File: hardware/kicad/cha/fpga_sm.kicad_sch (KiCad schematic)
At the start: 26 parts, among them J3 CONF SM, U14 iCE40HX4K-TQ144, X2 25 MHz 3,3 V

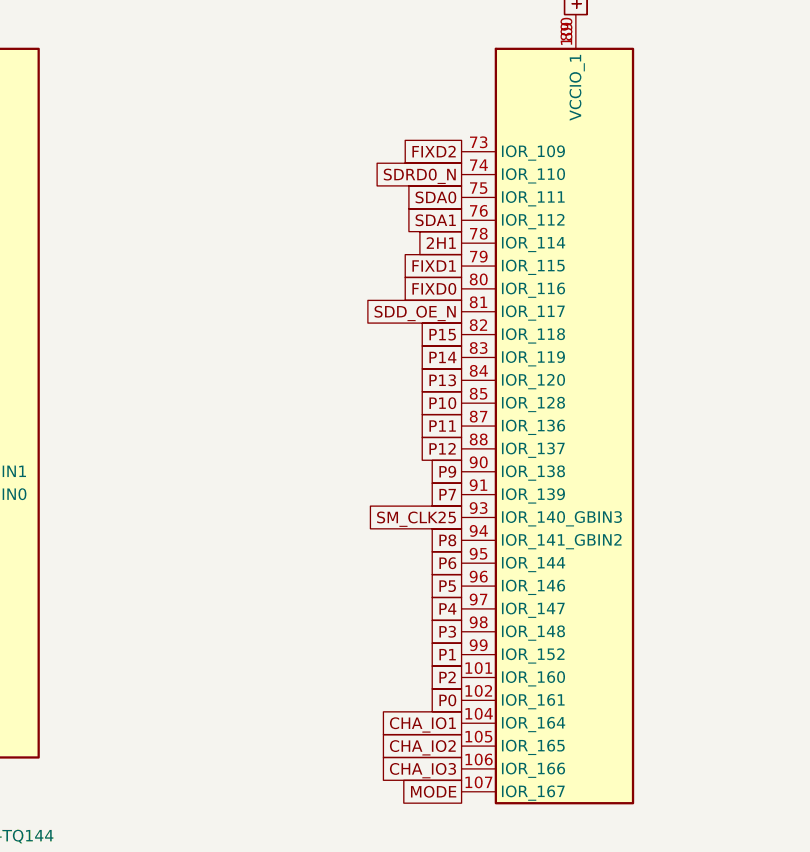
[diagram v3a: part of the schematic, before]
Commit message: CHA : canaux du tampon de sortie U7 groupés par FPGA source
Couche fixe (FPGA SM) puis sprites (FPGA C), chaque groupe dans l'ordre
des contacts : les deux groupes ne se croisent plus le long de la
rangée d'entrée du tampon, où les pistes FIXD enfermaient DOTA et GAD0.
Broches des FPGA C et SM réoptimisées, carte CHA régénérée (contrôle
Freerouting sans violation) ; nouveau routage en cours.

Co-Authored-By: Claude Opus 5.5 <noreply@anthropic.com>
Claude-Session: https://claude.ai/code/session_01WKfXP1YJ8otGxZ5dsY6Agh
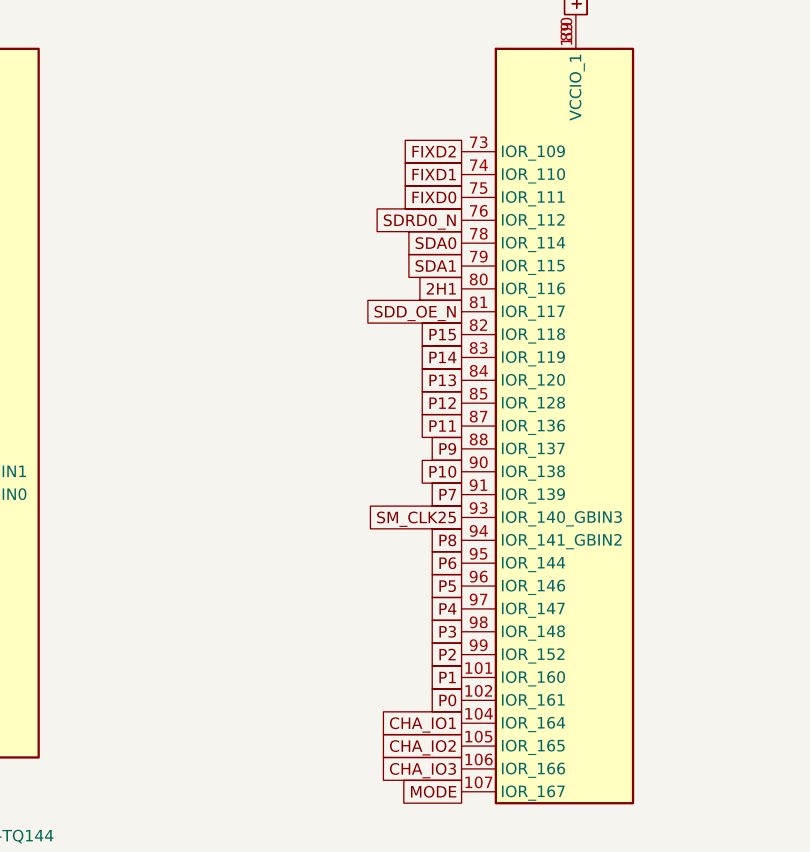
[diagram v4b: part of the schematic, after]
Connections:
- net 2H1: now also U14.80 (IOR_116); no longer U14.78 (IOR_114)
- net FIXD0: now also U14.75 (IOR_111); no longer U14.80 (IOR_116)
- net FIXD1: now also U14.74 (IOR_110); no longer U14.79 (IOR_115)
- net P1: now also U14.101 (IOR_160); no longer U14.99 (IOR_152)
- net P10: now also U14.90 (IOR_138); no longer U14.85 (IOR_128)
- net P12: now also U14.85 (IOR_128); no longer U14.88 (IOR_137)
- net P2: now also U14.99 (IOR_152); no longer U14.101 (IOR_160)
- net P9: now also U14.88 (IOR_137); no longer U14.90 (IOR_138)
- net SDA0: now also U14.78 (IOR_114); no longer U14.75 (IOR_111)
- net SDA1: now also U14.79 (IOR_115); no longer U14.76 (IOR_112)
- net SDRD0_N: now also U14.76 (IOR_112); no longer U14.74 (IOR_110)
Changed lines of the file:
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@@
     (instances
       (project "cha"
-        (path "/d4eaa97e-bb7e-46e6-b278-332026c2d879/3348bace-922d-4062-b9ed-5196f9aa129a"
+        (path "/c2acc1ad-3350-4022-8990-314ed37b470d/7c17e6ce-3dc1-4363-ae9a-1efd42617669"
           (reference "U14")
           (unit 1)))))
@@
     (instances
       (project "cha"
-        (path "/d4eaa97e-bb7e-46e6-b278-332026c2d879/3348bace-922d-4062-b9ed-5196f9aa129a"
+        (path "/c2acc1ad-3350-4022-8990-314ed37b470d/7c17e6ce-3dc1-4363-ae9a-1efd42617669"
           (reference "U14")
           (unit 2)))))
@@
         (font
           (size 1.27 1.27)) hide)))
-  (global_label "P2"
+  (global_label "P1"
     (shape passive)
     (at 121.92 111.76 180)
@@
         (font
           (size 1.27 1.27)) hide)))
-  (global_label "SDRD0_N"
+  (global_label "FIXD1"
     (shape passive)
     (at 121.92 55.88 180)
@@
         (font
           (size 1.27 1.27)) hide)))
-  (global_label "SDA0"
+  (global_label "FIXD0"
     (shape passive)
     (at 121.92 58.42 180)
@@
         (font
           (size 1.27 1.27)) hide)))
-  (global_label "SDA1"
+  (global_label "SDRD0_N"
     (shape passive)
     (at 121.92 60.96 180)
@@
         (font
           (size 1.27 1.27)) hide)))
-  (global_label "2H1"
+  (global_label "SDA0"
     (shape passive)
     (at 121.92 63.5 180)
@@
         (font
           (size 1.27 1.27)) hide)))
-  (global_label "FIXD1"
+  (global_label "SDA1"
     (shape passive)
     (at 121.92 66.04 180)
@@
         (font
           (size 1.27 1.27)) hide)))
-  (global_label "FIXD0"
+  (global_label "2H1"
     (shape passive)
     (at 121.92 68.58 180)
@@
         (font
           (size 1.27 1.27)) hide)))
-  (global_label "P10"
+  (global_label "P12"
     (shape passive)
     (at 121.92 81.28 180)
@@
         (font
           (size 1.27 1.27)) hide)))
-  (global_label "P12"
+  (global_label "P9"
     (shape passive)
     (at 121.92 86.36 180)
@@
         (font
           (size 1.27 1.27)) hide)))
-  (global_label "P9"
+  (global_label "P10"
     (shape passive)
     (at 121.92 88.9 180)
@@
         (font
           (size 1.27 1.27)) hide)))
-  (global_label "P1"
+  (global_label "P2"
     (shape passive)
     (at 121.92 109.22 180)
@@
     (instances
       (project "cha"
-        (path "/d4eaa97e-bb7e-46e6-b278-332026c2d879/3348bace-922d-4062-b9ed-5196f9aa129a"
+        (path "/c2acc1ad-3350-4022-8990-314ed37b470d/7c17e6ce-3dc1-4363-ae9a-1efd42617669"
           (reference "U14")
           (unit 3)))))
@@
     (instances
       (project "cha"
-        (path "/d4eaa97e-bb7e-46e6-b278-332026c2d879/3348bace-922d-4062-b9ed-5196f9aa129a"
+        (path "/c2acc1ad-3350-4022-8990-314ed37b470d/7c17e6ce-3dc1-4363-ae9a-1efd42617669"
           (reference "U14")
           (unit 4)))))
@@
     (instances
       (project "cha"
-        (path "/d4eaa97e-bb7e-46e6-b278-332026c2d879/3348bace-922d-4062-b9ed-5196f9aa129a"
+        (path "/c2acc1ad-3350-4022-8990-314ed37b470d/7c17e6ce-3dc1-4363-ae9a-1efd42617669"
           (reference "U14")
           (unit 5)))))
@@
     (instances
       (project "cha"
-        (path "/d4eaa97e-bb7e-46e6-b278-332026c2d879/3348bace-922d-4062-b9ed-5196f9aa129a"
+        (path "/c2acc1ad-3350-4022-8990-314ed37b470d/7c17e6ce-3dc1-4363-ae9a-1efd42617669"
           (reference "C50")
           (unit 1)))))
@@
     (instances
       (project "cha"
-        (path "/d4eaa97e-bb7e-46e6-b278-332026c2d879/3348bace-922d-4062-b9ed-5196f9aa129a"
+        (path "/c2acc1ad-3350-4022-8990-314ed37b470d/7c17e6ce-3dc1-4363-ae9a-1efd42617669"
           (reference "C51")
           (unit 1)))))
@@
     (instances
       (project "cha"
-        (path "/d4eaa97e-bb7e-46e6-b278-332026c2d879/3348bace-922d-4062-b9ed-5196f9aa129a"
+        (path "/c2acc1ad-3350-4022-8990-314ed37b470d/7c17e6ce-3dc1-4363-ae9a-1efd42617669"
           (reference "C52")
           (unit 1)))))
@@
     (instances
       (project "cha"
-        (path "/d4eaa97e-bb7e-46e6-b278-332026c2d879/3348bace-922d-4062-b9ed-5196f9aa129a"
+        (path "/c2acc1ad-3350-4022-8990-314ed37b470d/7c17e6ce-3dc1-4363-ae9a-1efd42617669"
           (reference "C53")
           (unit 1)))))
@@
     (instances
       (project "cha"
-        (path "/d4eaa97e-bb7e-46e6-b278-332026c2d879/3348bace-922d-4062-b9ed-5196f9aa129a"
+        (path "/c2acc1ad-3350-4022-8990-314ed37b470d/7c17e6ce-3dc1-4363-ae9a-1efd42617669"
           (reference "C54")
           (unit 1)))))
@@
     (instances
       (project "cha"
-        (path "/d4eaa97e-bb7e-46e6-b278-332026c2d879/3348bace-922d-4062-b9ed-5196f9aa129a"
+        (path "/c2acc1ad-3350-4022-8990-314ed37b470d/7c17e6ce-3dc1-4363-ae9a-1efd42617669"
           (reference "C55")
           (unit 1)))))
@@
     (instances
       (project "cha"
-        (path "/d4eaa97e-bb7e-46e6-b278-332026c2d879/3348bace-922d-4062-b9ed-5196f9aa129a"
+        (path "/c2acc1ad-3350-4022-8990-314ed37b470d/7c17e6ce-3dc1-4363-ae9a-1efd42617669"
           (reference "C56")
           (unit 1)))))
@@
     (instances
       (project "cha"
-        (path "/d4eaa97e-bb7e-46e6-b278-332026c2d879/3348bace-922d-4062-b9ed-5196f9aa129a"
+        (path "/c2acc1ad-3350-4022-8990-314ed37b470d/7c17e6ce-3dc1-4363-ae9a-1efd42617669"
           (reference "C57")
           (unit 1)))))
@@
     (instances
       (project "cha"
-        (path "/d4eaa97e-bb7e-46e6-b278-332026c2d879/3348bace-922d-4062-b9ed-5196f9aa129a"
+        (path "/c2acc1ad-3350-4022-8990-314ed37b470d/7c17e6ce-3dc1-4363-ae9a-1efd42617669"
           (reference "C58")
           (unit 1)))))
@@
     (instances
       (project "cha"
-        (path "/d4eaa97e-bb7e-46e6-b278-332026c2d879/3348bace-922d-4062-b9ed-5196f9aa129a"
+        (path "/c2acc1ad-3350-4022-8990-314ed37b470d/7c17e6ce-3dc1-4363-ae9a-1efd42617669"
           (reference "C59")
           (unit 1)))))
@@
     (instances
       (project "cha"
-        (path "/d4eaa97e-bb7e-46e6-b278-332026c2d879/3348bace-922d-4062-b9ed-5196f9aa129a"
+        (path "/c2acc1ad-3350-4022-8990-314ed37b470d/7c17e6ce-3dc1-4363-ae9a-1efd42617669"
           (reference "C60")
           (unit 1)))))
@@
     (instances
       (project "cha"
-        (path "/d4eaa97e-bb7e-46e6-b278-332026c2d879/3348bace-922d-4062-b9ed-5196f9aa129a"
+        (path "/c2acc1ad-3350-4022-8990-314ed37b470d/7c17e6ce-3dc1-4363-ae9a-1efd42617669"
           (reference "C61")
           (unit 1)))))
@@
     (instances
       (project "cha"
-        (path "/d4eaa97e-bb7e-46e6-b278-332026c2d879/3348bace-922d-4062-b9ed-5196f9aa129a"
+        (path "/c2acc1ad-3350-4022-8990-314ed37b470d/7c17e6ce-3dc1-4363-ae9a-1efd42617669"
           (reference "C62")
           (unit 1)))))
@@
     (instances
       (project "cha"
-        (path "/d4eaa97e-bb7e-46e6-b278-332026c2d879/3348bace-922d-4062-b9ed-5196f9aa129a"
+        (path "/c2acc1ad-3350-4022-8990-314ed37b470d/7c17e6ce-3dc1-4363-ae9a-1efd42617669"
           (reference "C63")
           (unit 1)))))
@@
     (instances
       (project "cha"
-        (path "/d4eaa97e-bb7e-46e6-b278-332026c2d879/3348bace-922d-4062-b9ed-5196f9aa129a"
+        (path "/c2acc1ad-3350-4022-8990-314ed37b470d/7c17e6ce-3dc1-4363-ae9a-1efd42617669"
           (reference "C64")
           (unit 1)))))
@@
     (instances
       (project "cha"
-        (path "/d4eaa97e-bb7e-46e6-b278-332026c2d879/3348bace-922d-4062-b9ed-5196f9aa129a"
+        (path "/c2acc1ad-3350-4022-8990-314ed37b470d/7c17e6ce-3dc1-4363-ae9a-1efd42617669"
           (reference "R10")
           (unit 1)))))
@@
     (instances
       (project "cha"
-        (path "/d4eaa97e-bb7e-46e6-b278-332026c2d879/3348bace-922d-4062-b9ed-5196f9aa129a"
+        (path "/c2acc1ad-3350-4022-8990-314ed37b470d/7c17e6ce-3dc1-4363-ae9a-1efd42617669"
           (reference "C65")
           (unit 1)))))
@@
     (instances
       (project "cha"
-        (path "/d4eaa97e-bb7e-46e6-b278-332026c2d879/3348bace-922d-4062-b9ed-5196f9aa129a"
+        (path "/c2acc1ad-3350-4022-8990-314ed37b470d/7c17e6ce-3dc1-4363-ae9a-1efd42617669"
           (reference "C66")
           (unit 1)))))
@@
     (instances
       (project "cha"
-        (path "/d4eaa97e-bb7e-46e6-b278-332026c2d879/3348bace-922d-4062-b9ed-5196f9aa129a"
+        (path "/c2acc1ad-3350-4022-8990-314ed37b470d/7c17e6ce-3dc1-4363-ae9a-1efd42617669"
           (reference "R11")
           (unit 1)))))
@@
     (instances
       (project "cha"
-        (path "/d4eaa97e-bb7e-46e6-b278-332026c2d879/3348bace-922d-4062-b9ed-5196f9aa129a"
+        (path "/c2acc1ad-3350-4022-8990-314ed37b470d/7c17e6ce-3dc1-4363-ae9a-1efd42617669"
           (reference "C67")
           (unit 1)))))
@@
     (instances
       (project "cha"
-        (path "/d4eaa97e-bb7e-46e6-b278-332026c2d879/3348bace-922d-4062-b9ed-5196f9aa129a"
+        (path "/c2acc1ad-3350-4022-8990-314ed37b470d/7c17e6ce-3dc1-4363-ae9a-1efd42617669"
           (reference "C68")
           (unit 1)))))
@@
     (instances
       (project "cha"
-        (path "/d4eaa97e-bb7e-46e6-b278-332026c2d879/3348bace-922d-4062-b9ed-5196f9aa129a"
+        (path "/c2acc1ad-3350-4022-8990-314ed37b470d/7c17e6ce-3dc1-4363-ae9a-1efd42617669"
           (reference "R12")
           (unit 1)))))
@@
     (instances
       (project "cha"
-        (path "/d4eaa97e-bb7e-46e6-b278-332026c2d879/3348bace-922d-4062-b9ed-5196f9aa129a"
+        (path "/c2acc1ad-3350-4022-8990-314ed37b470d/7c17e6ce-3dc1-4363-ae9a-1efd42617669"
           (reference "J3")
           (unit 1)))))
@@
     (instances
       (project "cha"
-        (path "/d4eaa97e-bb7e-46e6-b278-332026c2d879/3348bace-922d-4062-b9ed-5196f9aa129a"
+        (path "/c2acc1ad-3350-4022-8990-314ed37b470d/7c17e6ce-3dc1-4363-ae9a-1efd42617669"
           (reference "X2")
           (unit 1)))))
@@
     (instances
       (project "cha"
-        (path "/d4eaa97e-bb7e-46e6-b278-332026c2d879/3348bace-922d-4062-b9ed-5196f9aa129a"
+        (path "/c2acc1ad-3350-4022-8990-314ed37b470d/7c17e6ce-3dc1-4363-ae9a-1efd42617669"
           (reference "C69")
           (unit 1)))))
